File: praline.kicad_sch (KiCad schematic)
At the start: 0 parts

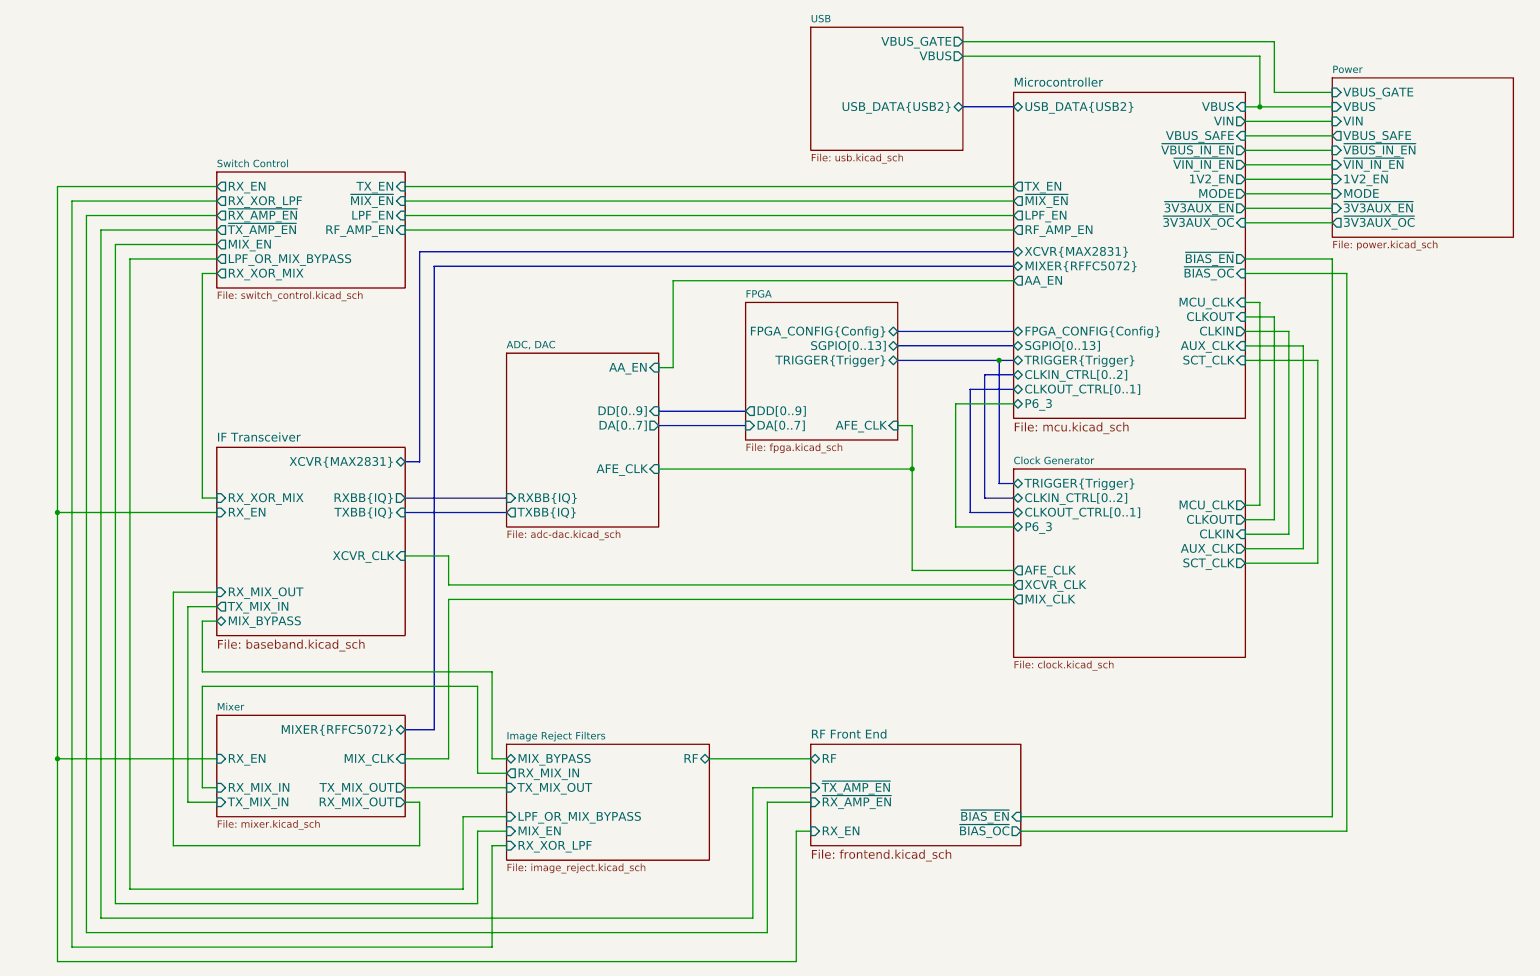
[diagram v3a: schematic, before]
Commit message: Add mixer loss compensation amplifiers
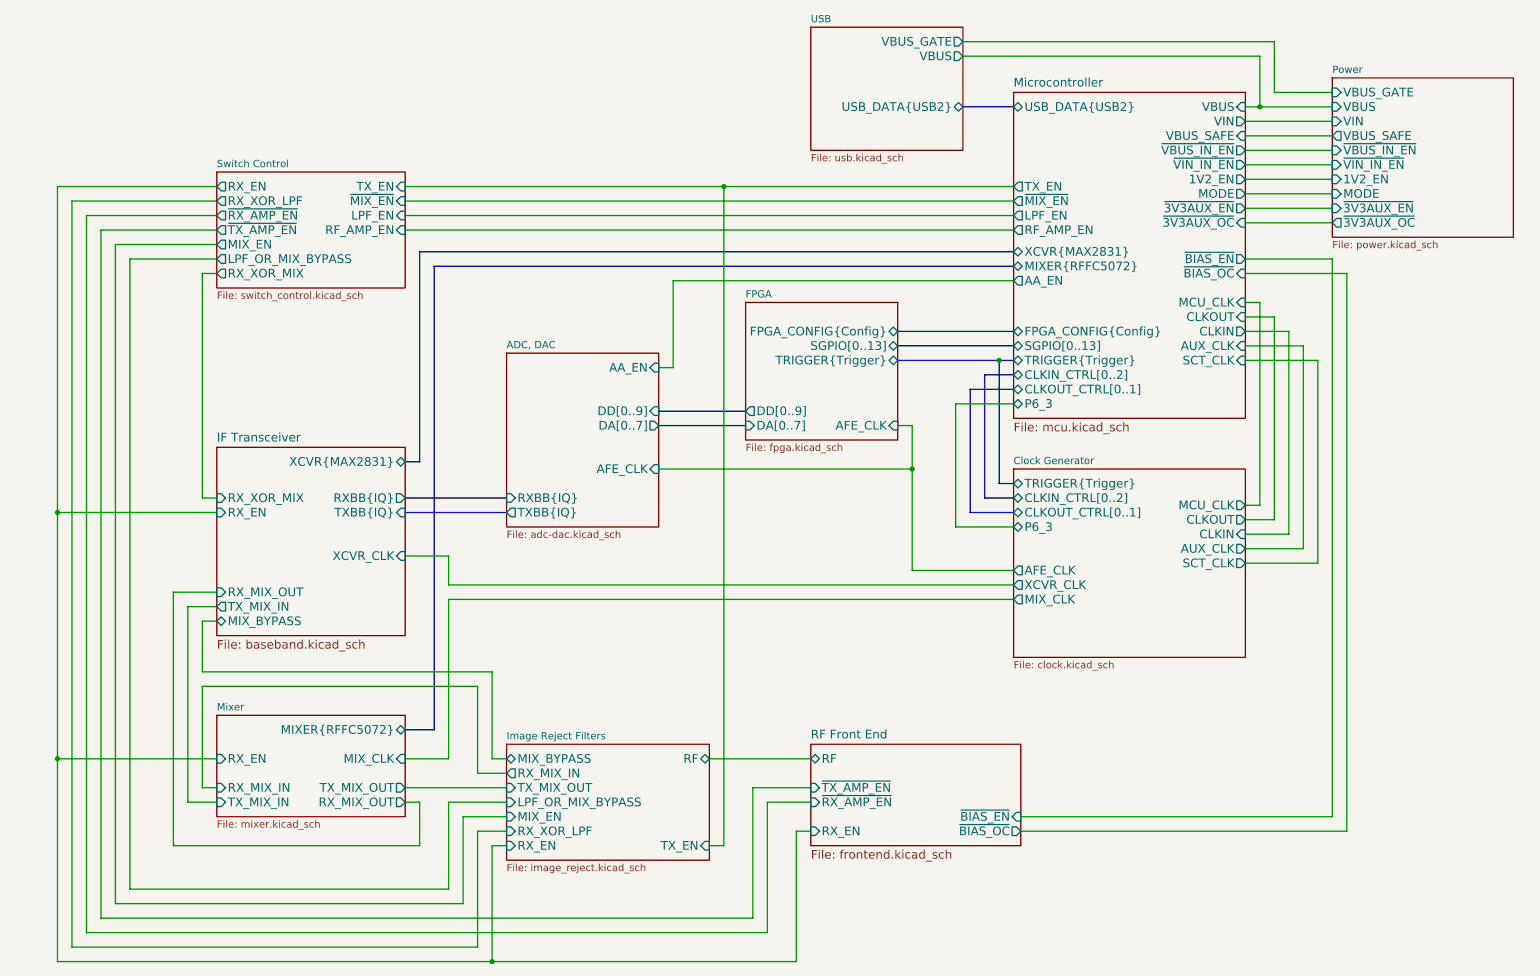
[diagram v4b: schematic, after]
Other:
- sheet Image Reject Filters ports: added RX_EN, TX_EN; removed none
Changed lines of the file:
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@@
+	)
+	(junction
+		(at 142.24 44.45)
+		(diameter 0)
+		(color 0 0 0 0)
 	)
 	(junction
@@
 	)
 	(junction
+		(at 101.6 180.34)
+		(diameter 0)
+		(color 0 0 0 0)
+	)
+	(junction
 		(at 25.4 101.6)
 		(diameter 0)
@@
 	(wire
 		(pts
+			(xy 101.6 180.34) (xy 25.4 180.34)
+		)
+		(stroke
+			(width 0)
+			(type default)
+		)
+	)
+	(wire
+		(pts
 			(xy 35.56 54.61) (xy 35.56 170.18)
 		)
@@
 	(wire
 		(pts
+			(xy 139.7 160.02) (xy 142.24 160.02)
+		)
+		(stroke
+			(width 0)
+			(type default)
+		)
+	)
+	(wire
+		(pts
+			(xy 101.6 180.34) (xy 101.6 160.02)
+		)
+		(stroke
+			(width 0)
+			(type default)
+		)
+	)
+	(wire
+		(pts
 			(xy 93.98 144.78) (xy 93.98 116.84)
 		)
@@
 	(wire
 		(pts
+			(xy 93.98 167.64) (xy 93.98 152.4)
+		)
+		(stroke
+			(width 0)
+			(type default)
+		)
+	)
+	(wire
+		(pts
 			(xy 48.26 118.11) (xy 48.26 152.4)
 		)
@@
 	(wire
 		(pts
-			(xy 86.36 44.45) (xy 193.04 44.45)
+			(xy 142.24 44.45) (xy 142.24 160.02)
+		)
+		(stroke
+			(width 0)
+			(type default)
+		)
+	)
+	(wire
+		(pts
+			(xy 86.36 44.45) (xy 142.24 44.45)
 		)
 		(stroke
@@
 	(wire
 		(pts
-			(xy 38.1 167.64) (xy 96.52 167.64)
-		)
-		(stroke
-			(width 0)
-			(type default)
-		)
-	)
-	(wire
-		(pts
-			(xy 35.56 170.18) (xy 99.06 170.18)
+			(xy 38.1 167.64) (xy 93.98 167.64)
+		)
+		(stroke
+			(width 0)
+			(type default)
+		)
+	)
+	(wire
+		(pts
+			(xy 35.56 170.18) (xy 96.52 170.18)
 		)
 		(stroke
@@
 	(wire
 		(pts
+			(xy 99.06 157.48) (xy 104.14 157.48)
+		)
+		(stroke
+			(width 0)
+			(type default)
+		)
+	)
+	(wire
+		(pts
 			(xy 175.26 86.36) (xy 175.26 93.98)
 		)
@@
 	(wire
 		(pts
-			(xy 99.06 157.48) (xy 104.14 157.48)
-		)
-		(stroke
-			(width 0)
-			(type default)
-		)
-	)
-	(wire
-		(pts
 			(xy 233.68 100.33) (xy 236.22 100.33)
 		)
@@
 	(wire
 		(pts
+			(xy 101.6 160.02) (xy 104.14 160.02)
+		)
+		(stroke
+			(width 0)
+			(type default)
+		)
+	)
+	(wire
+		(pts
 			(xy 27.94 46.99) (xy 53.34 46.99)
 		)
@@
 	(wire
 		(pts
-			(xy 99.06 170.18) (xy 99.06 157.48)
-		)
-		(stroke
-			(width 0)
-			(type default)
-		)
-	)
-	(wire
-		(pts
 			(xy 53.34 99.06) (xy 50.8 99.06)
 		)
@@
 	(wire
 		(pts
-			(xy 96.52 167.64) (xy 96.52 154.94)
-		)
-		(stroke
-			(width 0)
-			(type default)
-		)
-	)
-	(wire
-		(pts
 			(xy 50.8 132.08) (xy 50.8 149.86)
 		)
@@
 	(wire
 		(pts
+			(xy 93.98 152.4) (xy 104.14 152.4)
+		)
+		(stroke
+			(width 0)
+			(type default)
+		)
+	)
+	(wire
+		(pts
 			(xy 101.6 144.78) (xy 104.14 144.78)
 		)
@@
 	(wire
 		(pts
+			(xy 142.24 44.45) (xy 193.04 44.45)
+		)
+		(stroke
+			(width 0)
+			(type default)
+		)
+	)
+	(wire
+		(pts
 			(xy 101.6 129.54) (xy 101.6 144.78)
 		)
@@
 	(wire
 		(pts
+			(xy 99.06 177.8) (xy 99.06 157.48)
+		)
+		(stroke
+			(width 0)
+			(type default)
+		)
+	)
+	(wire
+		(pts
 			(xy 86.36 152.4) (xy 88.9 152.4)
 		)
@@
 	(wire
 		(pts
-			(xy 101.6 160.02) (xy 104.14 160.02)
-		)
-		(stroke
-			(width 0)
-			(type default)
-		)
-	)
-	(wire
-		(pts
 			(xy 99.06 132.08) (xy 50.8 132.08)
 		)
@@
 	(wire
 		(pts
-			(xy 101.6 177.8) (xy 27.94 177.8)
+			(xy 99.06 177.8) (xy 27.94 177.8)
 		)
 		(stroke
@@
 	(wire
 		(pts
+			(xy 96.52 154.94) (xy 104.14 154.94)
+		)
+		(stroke
+			(width 0)
+			(type default)
+		)
+	)
+	(wire
+		(pts
 			(xy 93.98 114.3) (xy 93.98 109.22)
 		)
@@
 		)
 	)
-	(wire
-		(pts
-			(xy 101.6 177.8) (xy 101.6 160.02)
-		)
-		(stroke
-			(width 0)
-			(type default)
-		)
-	)
 	(bus
 		(pts
@@
 	(wire
 		(pts
-			(xy 154.94 180.34) (xy 25.4 180.34)
+			(xy 154.94 180.34) (xy 101.6 180.34)
 		)
 		(stroke
@@
 	(wire
 		(pts
+			(xy 96.52 170.18) (xy 96.52 154.94)
+		)
+		(stroke
+			(width 0)
+			(type default)
+		)
+	)
+	(wire
+		(pts
 			(xy 50.8 149.86) (xy 53.34 149.86)
 		)
@@
 		(pts
 			(xy 86.36 101.6) (xy 104.14 101.6)
-		)
-		(stroke
-			(width 0)
-			(type default)
-		)
-	)
-	(wire
-		(pts
-			(xy 96.52 154.94) (xy 104.14 154.94)
 		)
 		(stroke
@@
 		)
 		(pin "RX_XOR_LPF" input
-			(at 104.14 160.02 180)
+			(at 104.14 157.48 180)
 			(effects
 				(font
@@
 		)
 		(pin "MIX_EN" input
-			(at 104.14 157.48 180)
+			(at 104.14 154.94 180)
 			(effects
 				(font
@@
 		)
 		(pin "LPF_OR_MIX_BYPASS" input
-			(at 104.14 154.94 180)
+			(at 104.14 152.4 180)
 			(effects
 				(font
@@
 			(effects
 				(font
+					(size 1.524 1.524)
+				)
+				(justify right)
+			)
+		)
+		(pin "RX_EN" input
+			(at 104.14 160.02 180)
+			(effects
+				(font
+					(size 1.524 1.524)
+				)
+				(justify left)
+			)
+		)
+		(pin "TX_EN" input
+			(at 139.7 160.02 0)
+			(effects
+				(font

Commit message: Add M2 mounting holes
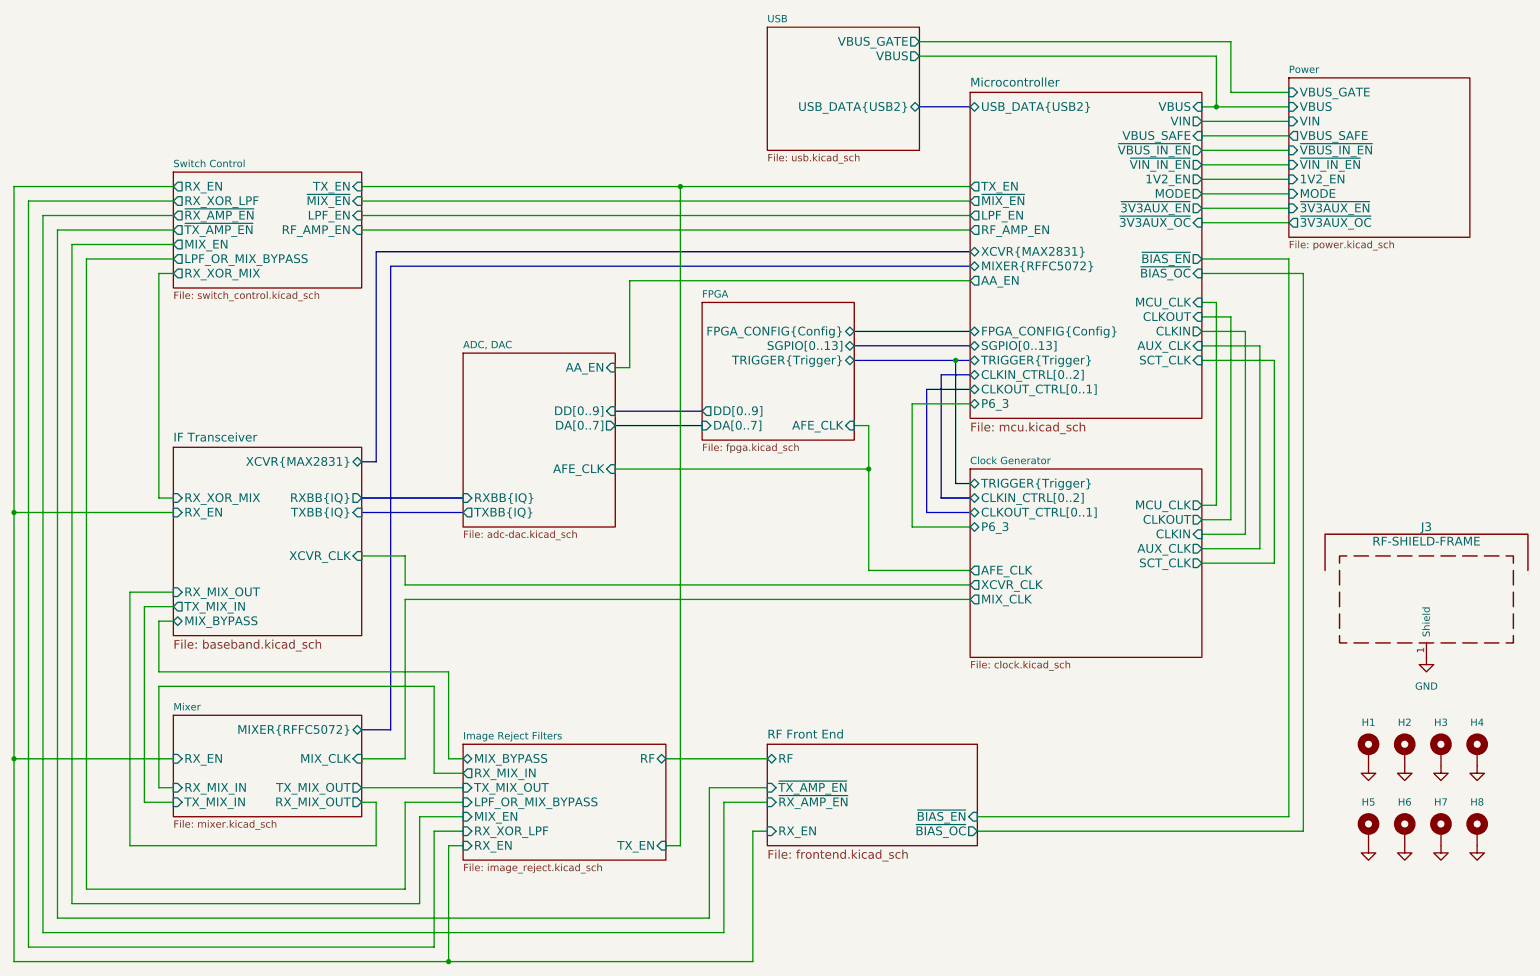
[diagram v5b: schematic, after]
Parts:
- added H1, H2, H3, H4: MountingHole_Pad, praline:MountingHole_3.2mm_M3_Pad_Via, symbol Mechanical:MountingHole_Pad
- added H5, H6, H7, H8: MountingHole_Pad, MountingHole:MountingHole_2.2mm_M2_Pad_Via, symbol Mechanical:MountingHole_Pad
- added J3: RF-SHIELD-FRAME, praline:Laird_Technologies_BMI-S-230-F_50.8x38.1mm, symbol Device:RFShield_TwoPieces
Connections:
- new net GND: H1.1, H2.1, H3.1, H4.1, H5.1, H6.1, H7.1, H8.1, J3.1 (Shield)

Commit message: Replace mixer compensation amps with single BGB741
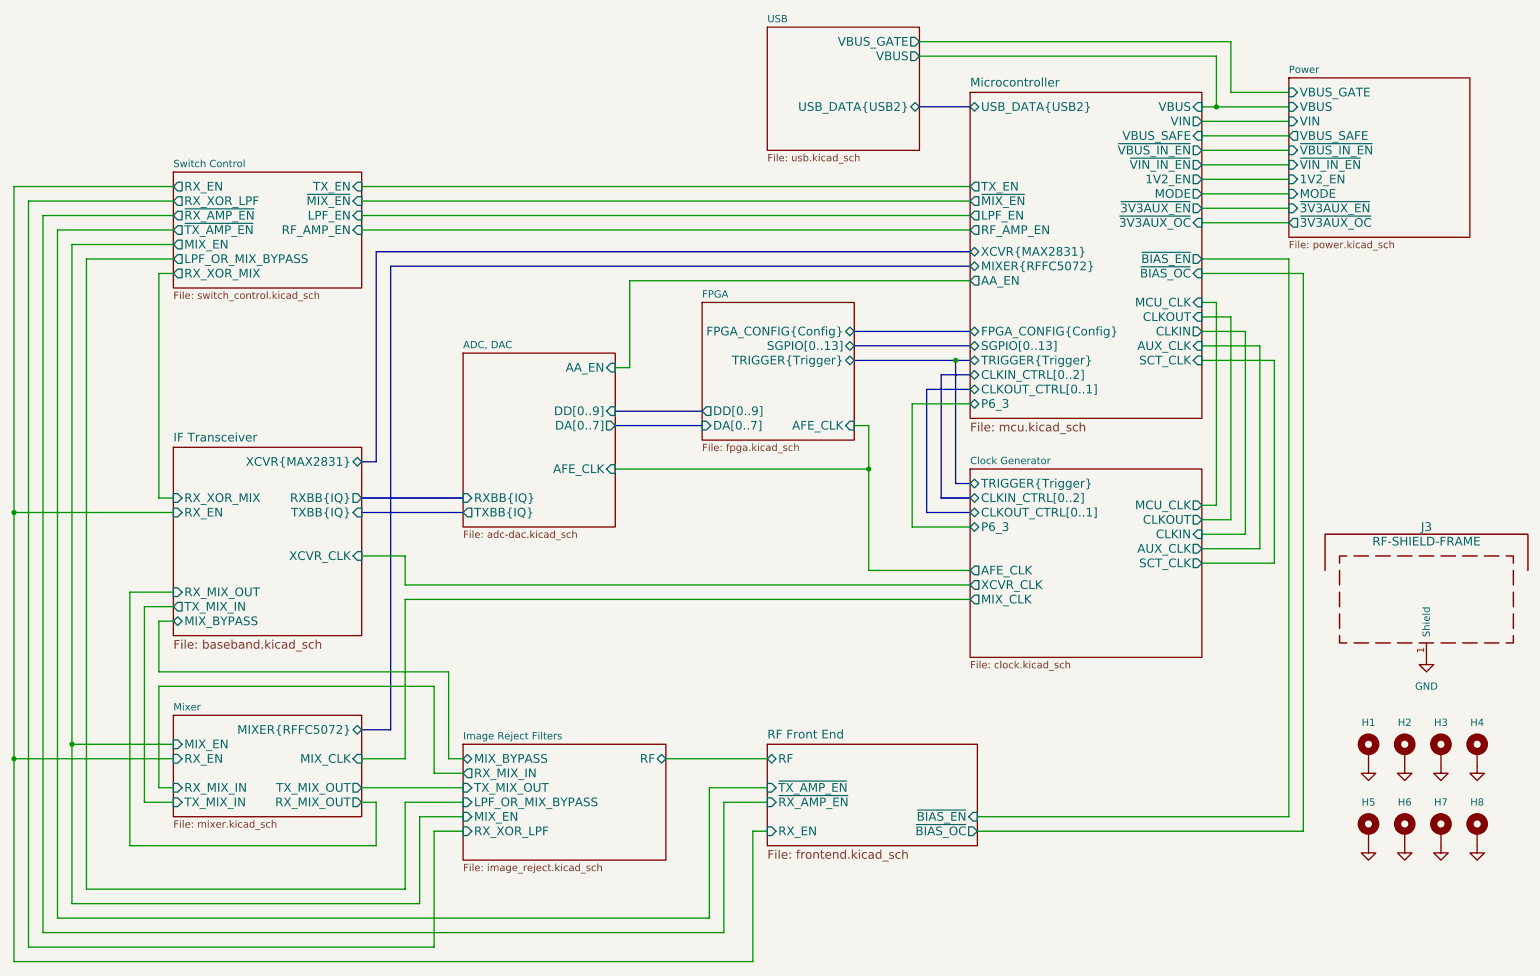
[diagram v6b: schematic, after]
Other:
- sheet Image Reject Filters ports: added none; removed RX_EN, TX_EN
- sheet Mixer ports: added MIX_EN; removed none
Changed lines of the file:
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@@
 	)
 	(junction
-		(at 134.62 44.45)
-		(diameter 0)
-		(color 0 0 0 0)
-	)
-	(junction
 		(at 167.64 93.98)
 		(diameter 0)
@@
 	)
 	(junction
-		(at 93.98 180.34)
+		(at 17.78 101.6)
 		(diameter 0)
 		(color 0 0 0 0)
 	)
 	(junction
-		(at 17.78 101.6)
+		(at 27.94 142.24)
 		(diameter 0)
 		(color 0 0 0 0)
@@
 	(wire
 		(pts
-			(xy 93.98 180.34) (xy 17.78 180.34)
-		)
-		(stroke
-			(width 0)
-			(type default)
-		)
-	)
-	(wire
-		(pts
-			(xy 27.94 54.61) (xy 27.94 170.18)
+			(xy 27.94 54.61) (xy 27.94 142.24)
 		)
 		(stroke
@@
 	(wire
 		(pts
-			(xy 132.08 160.02) (xy 134.62 160.02)
-		)
-		(stroke
-			(width 0)
-			(type default)
-		)
-	)
-	(wire
-		(pts
-			(xy 93.98 180.34) (xy 93.98 160.02)
-		)
-		(stroke
-			(width 0)
-			(type default)
-		)
-	)
-	(wire
-		(pts
 			(xy 86.36 144.78) (xy 86.36 116.84)
 		)
@@
 	(wire
 		(pts
-			(xy 134.62 44.45) (xy 134.62 160.02)
-		)
-		(stroke
-			(width 0)
-			(type default)
-		)
-	)
-	(wire
-		(pts
-			(xy 78.74 44.45) (xy 134.62 44.45)
+			(xy 78.74 44.45) (xy 185.42 44.45)
 		)
 		(stroke
@@
 	(wire
 		(pts
-			(xy 93.98 160.02) (xy 96.52 160.02)
-		)
-		(stroke
-			(width 0)
-			(type default)
-		)
-	)
-	(wire
-		(pts
 			(xy 20.32 46.99) (xy 45.72 46.99)
 		)
@@
 	(wire
 		(pts
-			(xy 134.62 44.45) (xy 185.42 44.45)
+			(xy 27.94 142.24) (xy 27.94 170.18)
 		)
 		(stroke
@@
 		)
 	)
+	(wire
+		(pts
+			(xy 27.94 142.24) (xy 45.72 142.24)
+		)
+		(stroke
+			(width 0)
+			(type default)
+		)
+	)
 	(bus
 		(pts
@@
 	(wire
 		(pts
-			(xy 147.32 180.34) (xy 93.98 180.34)
+			(xy 17.78 180.34) (xy 147.32 180.34)
 		)
 		(stroke
@@
 			)
 		)
+		(pin "MIX_EN" input
+			(at 45.72 142.24 180)
+			(effects
+				(font
+					(size 1.524 1.524)
+				)
+				(justify left)
+			)
+		)
 		(instances
 			(project "praline"
@@
 			(effects
 				(font
-					(size 1.524 1.524)
-				)
-				(justify right)
-			)
-		)
-		(pin "RX_EN" input
-			(at 96.52 160.02 180)
-			(effects
-				(font
-					(size 1.524 1.524)
-				)
-				(justify left)
-			)
-		)
-		(pin "TX_EN" input
-			(at 132.08 160.02 0)
-			(effects
-				(font
